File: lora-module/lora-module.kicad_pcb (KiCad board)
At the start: 2 copper layers, 86 x 31 mm, 28 parts, among them J1 North, J2 South, J3 West, J4 East, J5 Conn_Coaxial, U3 BA033CC0FP-E2, U4 MAX3486, U5 MAX3486, U7 RFM95W-868S2

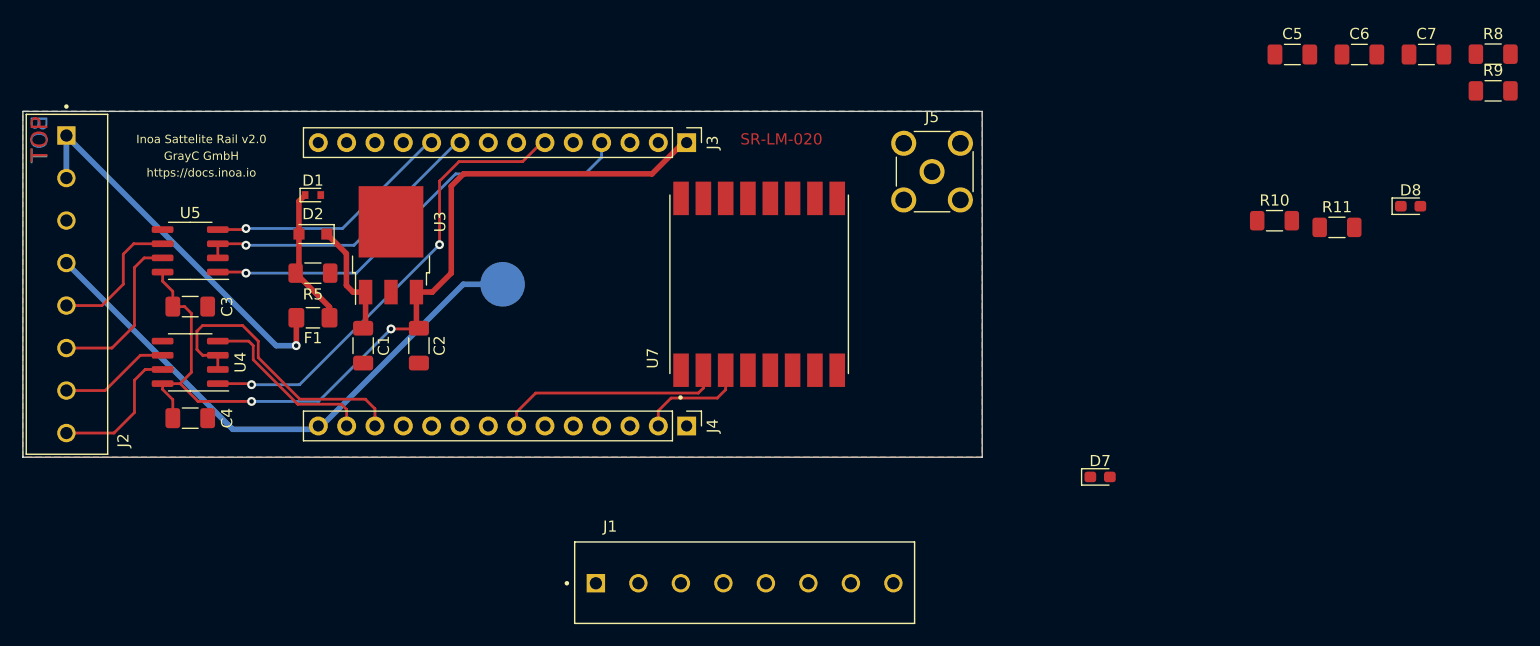
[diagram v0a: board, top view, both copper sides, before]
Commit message: Added SMA connector for LoRa module
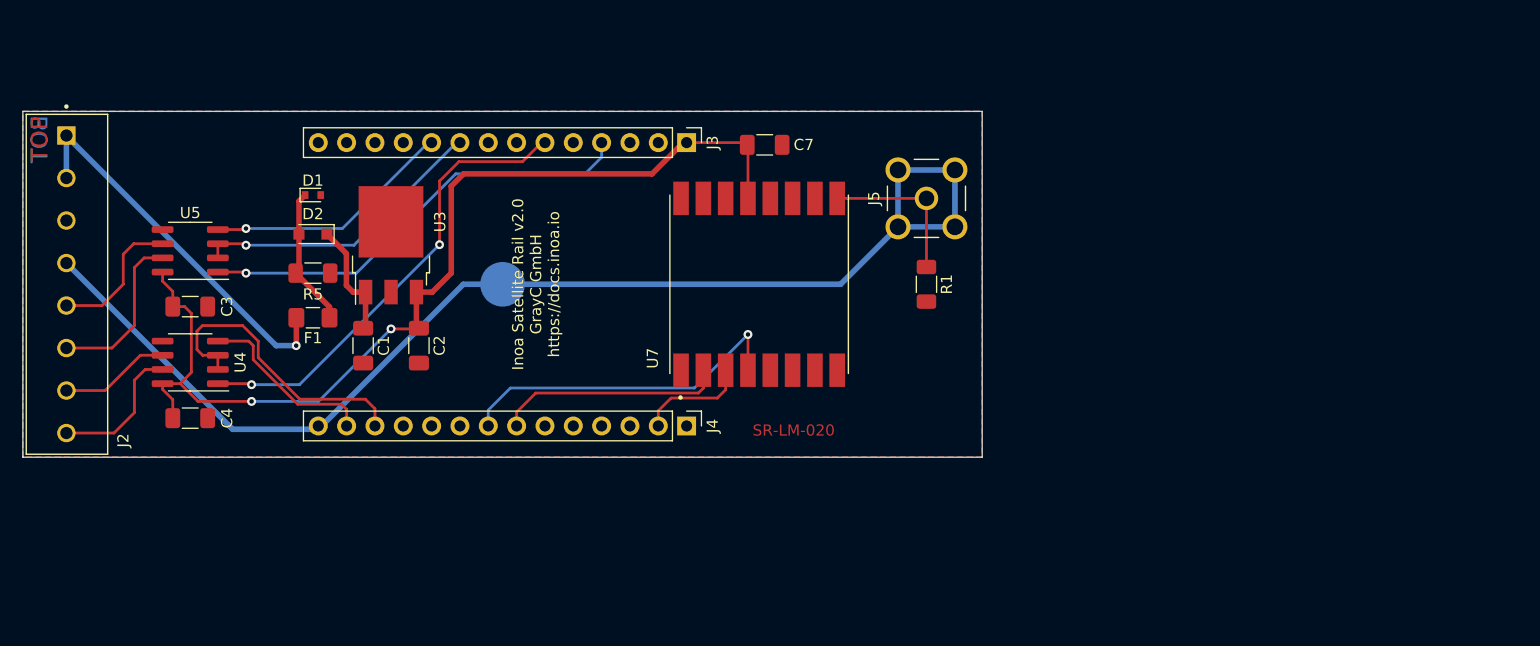
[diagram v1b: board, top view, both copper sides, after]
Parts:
- removed C5, C6: 100nF, Capacitor_SMD:C_1206_3216Metric_Pad1.33x1.80mm_HandSolder
- removed D7, D8: D_TVS, Diode_SMD:D_0603_1608Metric_Pad1.05x0.95mm_HandSolder
- removed J1: North, footprints:PHOENIX_1727078
- removed R10, R11: 220R, Resistor_SMD:R_1206_3216Metric_Pad1.30x1.75mm_HandSolder
- removed R8, R9: 10k, Resistor_SMD:R_1206_3216Metric_Pad1.30x1.75mm_HandSolder
- added R1: 220R, Resistor_SMD:R_1206_3216Metric_Pad1.30x1.75mm_HandSolder, F.Cu at (181.0, 95.5)
- G1: moved to F.Cu
- J5: footprint Connector_Coaxial:SMA_Molex_73251-2200_Horizontal -> footprints:LINX_CONSMA002
- moved C7 59.9 mm to (166.5, 83.0)
- moved J5 2.45 mm to (181.0, 87.8), turned to 90 degrees
- moved G1 1.00 mm to (115.0, 84.0), turned to 0 degrees
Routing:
- net GNDPWR: track 50.7 -> 108.6 mm
- net SPI_0_CLK: track 0.00 -> 30.7 mm, vias 0 -> 1
- net Net-(J5-Pad1): track 0.00 -> 14.2 mm
- net +3V3: track 79.9 -> 90.2 mm
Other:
- board text added: "Inoa Satellite Rail v2.0 GrayC GmbH https://docs.inoa.io"
- board text removed: "GrayC GmbH"
- board text removed: "Inoa Sattelite Rail v2.0"
- board text removed: "https://docs.inoa.io"

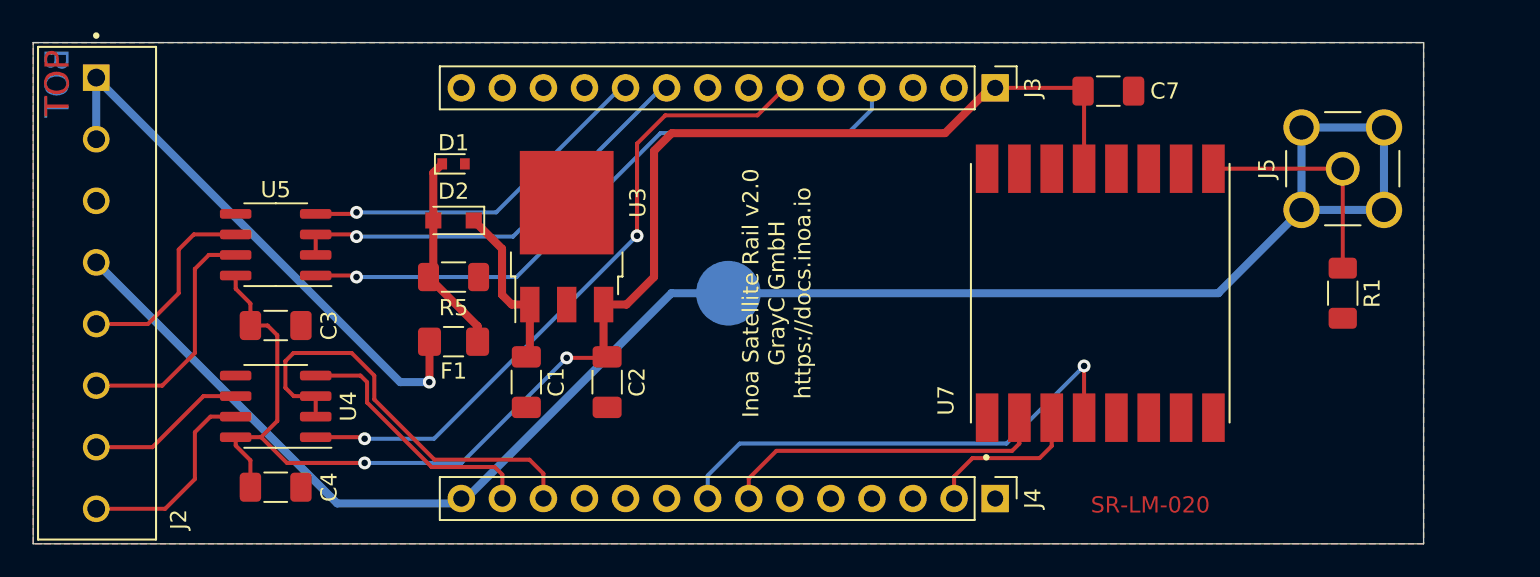
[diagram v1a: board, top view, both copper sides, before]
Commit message: Ongoing work LoRa module
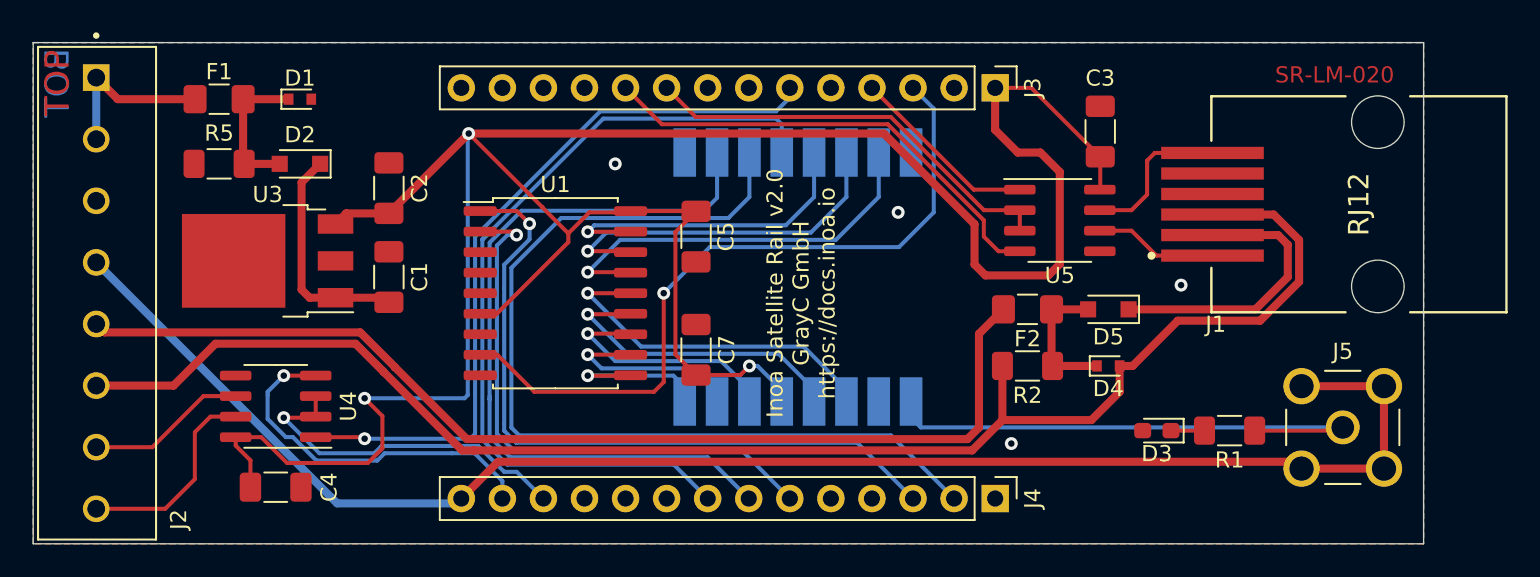
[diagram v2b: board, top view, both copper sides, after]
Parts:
- removed TP1: Shield, TestPoint:TestPoint_Pad_D4.0mm
- added C5: 100nF, Capacitor_SMD:C_1206_3216Metric_Pad1.33x1.80mm_HandSolder, F.Cu at (141.0, 92.0)
- added D3: D_TVS, Diode_SMD:D_0603_1608Metric_Pad1.05x0.95mm_HandSolder, F.Cu at (169.5, 104.0)
- added D4: 25V, Diode_SMD:D_SOD-523, F.Cu at (166.5, 100.0)
- added D5: 1N5819, Diode_SMD:D_SOD-323_HandSoldering, F.Cu at (166.5, 96.5)
- added F2: 23V/2A, Fuse:Fuse_1206_3216Metric_Pad1.42x1.75mm_HandSolder, F.Cu at (161.5, 96.5)
- added J1: RJ12, footprints:Molex-95501-6669-MFG, F.Cu at (182.0, 90.0)
- added R2: 10k, Resistor_SMD:R_1206_3216Metric_Pad1.30x1.75mm_HandSolder, F.Cu at (161.5, 100.0)
- added U1: MCP23008-xSO, Package_SO:SOIC-18W_7.5x11.6mm_P1.27mm, F.Cu at (132.3, 95.5)
- C1: value 100nF / 35V -> 100nF/35V
- U7: moved to B.Cu
- moved C3 52.4 mm to (166.0, 85.5), turned to 90 degrees
- moved U5 48.5 mm to (163.5, 91.0), turned to 0 degrees
- moved G1 40.2 mm to (153.5, 95.5), turned to 90 degrees
- moved C7 30.1 mm to (141.0, 99.0), turned to 90 degrees
- moved F1 20.9 mm to (111.5, 83.5)
- moved U7 18.7 mm to (147.3, 94.5), turned to 270 degrees
- moved U3 18.6 mm to (114.5, 93.5), turned to 180 degrees
- moved C2 18.1 mm to (122.0, 89.0), turned to 90 degrees
- moved R5 16.1 mm to (111.5, 87.5), turned to 180 degrees
- moved J5 16.0 mm to (181.0, 103.8)
- moved R1 11.0 mm to (174.0, 104.0), turned to 180 degrees
- moved C1 10.7 mm to (122.0, 94.5), turned to 90 degrees
- moved D1 10.3 mm to (116.5, 83.5)
- moved D2 10.1 mm to (116.5, 87.5)
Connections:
- J2 pad 5: RS485_0_A -> VBUS
- J2 pad 6: RS485_0_B -> GND1
- J3 pad 3: Net-(J3-Pad3) -> I2C_Int
- U7 pad 11: Net-(U7-Pad11) -> LoRa_DIO3
- U7 pad 12: Net-(U7-Pad12) -> LoRa_DIO4
- U7 pad 14: Net-(U7-Pad14) -> LoRa_DIO0
- U7 pad 15: Net-(U7-Pad15) -> LoRa_DIO1
- U7 pad 16: Net-(U7-Pad16) -> LoRa_DIO2
- U7 pad 5: Net-(U7-Pad5) -> LoRa_CS
- U7 pad 6: Net-(U7-Pad6) -> LoRa_Reset
- U7 pad 7: Net-(U7-Pad7) -> LoRa_DIO5
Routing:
- net GND1: track 0.00 -> 95.4 mm
- net +3V3: track 90.2 -> 160.1 mm, vias 2 -> 3
- net VBUS: track 0.00 -> 65.8 mm
- net SPI_0_MOSI: track 9.93 -> 57.4 mm
- net I2C_Int: track 0.00 -> 45.0 mm, vias 0 -> 1
- net I2C_SCL: track 0.00 -> 43.9 mm, vias 0 -> 1
- net I2C_SDA: track 0.00 -> 35.2 mm, vias 0 -> 1
- net RS485_0_RX: track 40.4 -> 11.8 mm, vias 1 -> 0
- net SPI_0_MISO: track 20.5 -> 47.1 mm
- net LoRa_DIO5: track 0.00 -> 24.3 mm, vias 0 -> 1
- net VCC: track 34.7 -> 10.5 mm, vias 1 -> 0
- net LoRa_DIO3: track 0.00 -> 22.9 mm, vias 0 -> 1
- net SPI_0_CLK: track 30.7 -> 53.2 mm, vias 1 -> 0
- net LoRa_Reset: track 0.00 -> 21.8 mm, vias 0 -> 1
- net LoRa_DIO4: track 0.00 -> 20.3 mm, vias 0 -> 1
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
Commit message: Added OpenHardware Logo to PCBs
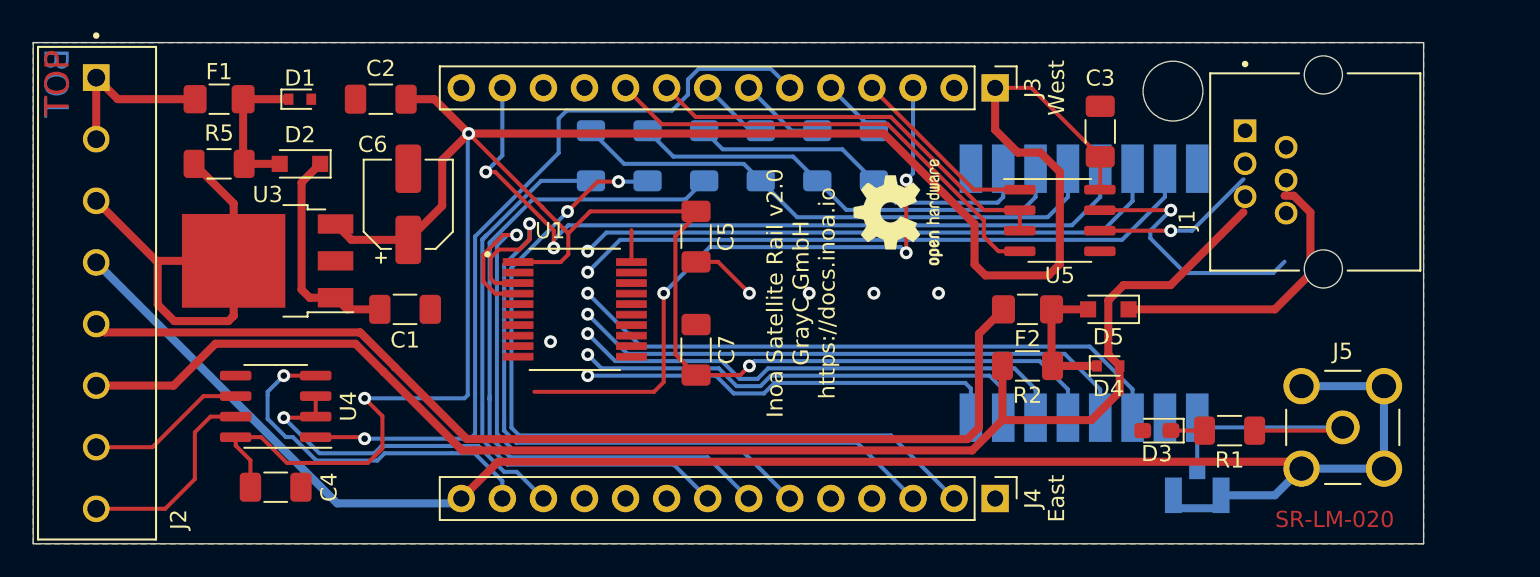
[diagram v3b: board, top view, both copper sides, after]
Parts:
- added C6: 47uF, Capacitor_SMD:CP_Elec_5x5.3, F.Cu at (123.2, 90.0)
- added G2: Logo_Open_Hardware_Small, Symbol:OSHW-Logo2_7.3x6mm_SilkScreen, F.Cu at (153.5, 90.5)
- added H1: Antenna, MountingHole:MountingHole_3.7mm, F.Cu at (170.5, 83.0)
- added J6: LoRa I-PEX, footprints:SAMTEC_RSP-122811-01, B.Cu at (172.0, 108.0)
- added R3: 0R, Resistor_SMD:R_1206_3216Metric_Pad1.30x1.75mm_HandSolder, B.Cu at (152.0, 87.0)
- added R4: 0R, Resistor_SMD:R_1206_3216Metric_Pad1.30x1.75mm_HandSolder, B.Cu at (148.5, 87.0)
- added R6: 0R, Resistor_SMD:R_1206_3216Metric_Pad1.30x1.75mm_HandSolder, B.Cu at (145.0, 87.0)
- added R7: 0R, Resistor_SMD:R_1206_3216Metric_Pad1.30x1.75mm_HandSolder, B.Cu at (138.0, 87.0)
- added R8: 0R, Resistor_SMD:R_1206_3216Metric_Pad1.30x1.75mm_HandSolder, B.Cu at (141.5, 87.0)
- added R9: 0R, Resistor_SMD:R_1206_3216Metric_Pad1.30x1.75mm_HandSolder, B.Cu at (134.5, 87.0)
- C2: value 100nF -> 0u1
- D4: value 25V -> 13V
- F2: value 23V/2A -> 13V/2A
- J1: footprint footprints:Molex-95501-6669-MFG -> footprints:CUI_CRJ030-G-TH
- J5: value Conn_Coaxial -> LoRa SMA
- U1: value MCP23008-xSO -> MCP23009-E_SS; footprint Package_SO:SOIC-18W_7.5x11.6mm_P1.27mm -> footprints:SOP65P780X200-20N
- moved U7 17.7 mm to (165.0, 95.5)
- moved C2 5.52 mm to (121.5, 83.5), turned to 180 degrees
- moved G1 5.00 mm to (153.5, 100.5)
- moved J1 2.97 mm to (179.8, 88.0)
- moved C1 2.24 mm to (123.0, 96.5), turned to 0 degrees
- moved U1 1.56 mm to (133.5, 96.5)
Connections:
- J3 pad 13: Net-(J3-Pad13) -> LoRa_CS
- J4 pad 2: SPI_0_MOSI -> Net-(J4-Pad2)
- J4 pad 7: SPI_0_MISO -> Net-(J4-Pad7)
- J4 pad 8: SPI_0_CLK -> Net-(J4-Pad8)
- U1 pad 1: I2C_SCL -> +3V3
- U1 pad 10: LoRa_DIO2 -> (no net)
- U1 pad 11: LoRa_DIO1 -> (no net)
- U1 pad 12: LoRa_DIO0 -> Net-(U1-Pad12)
- U1 pad 13: LoRa_DIO4 -> Net-(U1-Pad13)
- U1 pad 14: LoRa_DIO3 -> Net-(U1-Pad14)
- U1 pad 15: LoRa_DIO5 -> Net-(U1-Pad15)
- U1 pad 16: LoRa_Reset -> Net-(U1-Pad16)
- U1 pad 17: LoRa_CS -> Net-(U1-Pad17)
- U1 pad 18: +3V3 -> (no net)
- U1 pad 2: I2C_SDA -> (no net)
- U1 pad 3: GND -> I2C_SCL
- U1 pad 4: GND -> I2C_SDA
- U1 pad 5: GND -> Net-(U1-Pad5)
- U1 pad 6: +3V3 -> Net-(U1-Pad6)
- U1 pad 7: Net-(U1-Pad7) -> I2C_Int
- U1 pad 8: I2C_Int -> LoRa_DIO2
- U1 pad 9: GND -> LoRa_DIO1
- U7 pad 2: SPI_0_MISO -> SPI_MISO
- U7 pad 3: SPI_0_MOSI -> SPI_MOSI
- U7 pad 4: SPI_0_CLK -> SPI_CLK
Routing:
- net SPI_0_MOSI: track 57.4 -> 0.00 mm
- net SPI_0_CLK: track 53.2 -> 0.00 mm
- net Net-(J4-Pad2): track 0.00 -> 49.7 mm, vias 0 -> 2
- net SPI_0_MISO: track 47.1 -> 0.00 mm
- net Net-(J4-Pad7): track 0.00 -> 44.9 mm
- net Net-(J4-Pad8): track 0.00 -> 36.4 mm
- net GND: track 0.00 -> 34.2 mm, vias 4 -> 5
- net SPI_CLK: track 0.00 -> 34.0 mm
- net LoRa_CS: track 19.3 -> 49.5 mm, vias 1 -> 2
- net SPI_MOSI: track 0.00 -> 28.1 mm
- net +3V3: track 160.1 -> 182.5 mm
- net SPI_MISO: track 0.00 -> 22.2 mm
- net LoRa_DIO1: track 13.3 -> 28.9 mm
- net LoRa_DIO0: track 15.8 -> 31.4 mm
- net LoRa_DIO2: track 10.8 -> 26.4 mm
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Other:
- board text added: "SPI_1_CLK"
- board text added: "SPI_1_MISO"
- board text added: "SPI_1_MOSI"
- board text added: "SPI_2_CLK"
- board text added: "SPI_2_MISO"
- board text added: "SPI_2_MOSI"

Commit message: Feature/kicad 6 migration (#2)
* Adjust CI/CD jobs to use KiCad 6

* Migrate panel module project

* Unify KiBot config

* Migrate Ethernet, SoC, Metering Modules to KiCad6

* Change build order to find out more about strange behavior

* Trigger build also on workflow changes

* Try to increase log level to track error

* Switch to KiCad 6 schematic files

* Fix / Ignore Errors in panel module

* Disable cost calculation for now

* Fixing more ERC errors

* Remove outdated files and settings

* Trim further warnings and errors

* Update documentation

* Migrate in-progress projects
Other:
- net class Default removed
